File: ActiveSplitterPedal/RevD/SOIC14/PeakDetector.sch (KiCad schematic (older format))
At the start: 11 parts, among them U3 TL074

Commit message: Completed RevD
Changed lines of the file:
@@
 AR Path="/5F6A4453/5F3F63C2" Ref="U9"  Part="2"
 AR Path="/5F6AEF1B/5F3F63C2" Ref="U12"  Part="2"
-F 0 "U6" H 4025 2925 50  0000 C CNN
+F 0 "U12" H 4025 2925 50  0000 C CNN
 F 1 "TL074" H 4025 2825 50  0000 C CNN
 F 2 "Package_SO:SOIC-14_3.9x8.7mm_P1.27mm" H 4000 2625 50  0001 C CNN
@@
 AR Path="/5F6A4453/5F3F8AC2" Ref="U9"  Part="4"
 AR Path="/5F6AEF1B/5F3F8AC2" Ref="U12"  Part="4"
-F 0 "U6" H 7700 3092 50  0000 C CNN
+F 0 "U12" H 7700 3092 50  0000 C CNN
 F 1 "TL074" H 7700 3001 50  0000 C CNN
 F 2 "Package_SO:SOIC-14_3.9x8.7mm_P1.27mm" H 7650 2825 50  0001 C CNN
@@
 AR Path="/5F6A4453/5F3F9579" Ref="U9"  Part="5"
 AR Path="/5F6AEF1B/5F3F9579" Ref="U12"  Part="5"
-F 0 "U6" H 2650 6025 50  0000 R CNN
+F 0 "U12" H 2650 6025 50  0000 R CNN
 F 1 "TL074" H 2700 5925 50  0000 R CNN
 F 2 "Package_SO:SOIC-14_3.9x8.7mm_P1.27mm" H 2450 6075 50  0001 C CNN
@@
 AR Path="/5F6A4453/5F44F4A6" Ref="C27"  Part="1"
 AR Path="/5F6AEF1B/5F44F4A6" Ref="C38"  Part="1"
-F 0 "C16" H 3215 6671 50  0000 L CNN
+F 0 "C38" H 3215 6671 50  0000 L CNN
 F 1 "100nF" H 3215 6580 50  0000 L CNN
 F 2 "Capacitor_SMD:C_0805_2012Metric_Pad1.15x1.40mm_HandSolder" H 3138 6475 50  0001 C CNN
@@
 AR Path="/5F6A4453/5F45B6FE" Ref="C26"  Part="1"
 AR Path="/5F6AEF1B/5F45B6FE" Ref="C37"  Part="1"
-F 0 "C15" H 3215 5896 50  0000 L CNN
+F 0 "C37" H 3215 5896 50  0000 L CNN
 F 1 "100nF" H 3215 5805 50  0000 L CNN
 F 2 "Capacitor_SMD:C_0805_2012Metric_Pad1.15x1.40mm_HandSolder" H 3138 5700 50  0001 C CNN
@@
 AR Path="/5F6A4453/5F4B9375" Ref="D6"  Part="1"
 AR Path="/5F6AEF1B/5F4B9375" Ref="D8"  Part="1"
-F 0 "D4" V 8539 3207 50  0000 R CNN
+F 0 "D8" V 8539 3207 50  0000 R CNN
 F 1 "LED" V 8448 3207 50  0000 R CNN
 F 2 "LED_THT:LED_D5.0mm" H 8500 3325 50  0001 C CNN
@@
 AR Path="/5F6A4453/5F57D775" Ref="R14"  Part="1"
 AR Path="/5F6AEF1B/5F57D775" Ref="R20"  Part="1"
-F 0 "R8" V 4100 3075 50  0000 R CNN
+F 0 "R20" V 4100 3075 50  0000 R CNN
 F 1 "120K" V 3900 3125 50  0000 R CNN
 F 2 "Resistor_SMD:R_0805_2012Metric_Pad1.15x1.40mm_HandSolder" V 3930 3025 50  0001 C CNN
@@
 AR Path="/5F6A4453/5F58191C" Ref="R13"  Part="1"
 AR Path="/5F6AEF1B/5F58191C" Ref="R19"  Part="1"
-F 0 "R7" H 3800 3575 50  0000 R CNN
+F 0 "R19" H 3800 3575 50  0000 R CNN
 F 1 "1K" H 3800 3675 50  0000 R CNN
 F 2 "Resistor_SMD:R_0805_2012Metric_Pad1.15x1.40mm_HandSolder" V 3530 3625 50  0001 C CNN
@@
 AR Path="/5F6A4453/5F579AC3" Ref="R15"  Part="1"
 AR Path="/5F6AEF1B/5F579AC3" Ref="R21"  Part="1"
-F 0 "R9" H 8430 2879 50  0000 R CNN
+F 0 "R21" H 8430 2879 50  0000 R CNN
 F 1 "220R" H 8430 2970 50  0000 R CNN
 F 2 "Resistor_SMD:R_0805_2012Metric_Pad1.15x1.40mm_HandSolder" V 8430 2925 50  0001 C CNN
@@
 AR Path="/5F6A4453/5F5A1DE7" Ref="U9"  Part="3"
 AR Path="/5F6AEF1B/5F5A1DE7" Ref="U12"  Part="3"
-F 0 "U6" H 4850 5700 50  0000 C CNN
+F 0 "U12" H 4850 5700 50  0000 C CNN
 F 1 "TL074" H 4850 5800 50  0000 C CNN
 F 2 "Package_SO:SOIC-14_3.9x8.7mm_P1.27mm" H 4800 6200 50  0001 C CNN
@@
 AR Path="/5F6A4453/5F59995E" Ref="#PWR0128"  Part="1"
 AR Path="/5F6AEF1B/5F59995E" Ref="#PWR0140"  Part="1"
-F 0 "#PWR0116" H 3100 6675 50  0001 C CNN
+F 0 "#PWR0140" H 3100 6675 50  0001 C CNN
 F 1 "VCOM" H 3115 6998 50  0000 C CNN
 F 2 "" H 3100 6825 50  0001 C CNN
@@
 AR Path="/5F6A4453/5F599E65" Ref="#PWR0129"  Part="1"
 AR Path="/5F6AEF1B/5F599E65" Ref="#PWR0141"  Part="1"
-F 0 "#PWR0117" H 3600 3725 50  0001 C CNN
+F 0 "#PWR0141" H 3600 3725 50  0001 C CNN
 F 1 "VCOM" H 3615 4048 50  0000 C CNN
 F 2 "" H 3600 3875 50  0001 C CNN
@@
 AR Path="/5F6A4453/5F59A32D" Ref="#PWR0130"  Part="1"
 AR Path="/5F6AEF1B/5F59A32D" Ref="#PWR0142"  Part="1"
-F 0 "#PWR0118" H 6525 3725 50  0001 C CNN
+F 0 "#PWR0142" H 6525 3725 50  0001 C CNN
 F 1 "VCOM" H 6540 4048 50  0000 C CNN
 F 2 "" H 6525 3875 50  0001 C CNN
@@
 AR Path="/5F6A4453/5F59A89E" Ref="#PWR0131"  Part="1"
 AR Path="/5F6AEF1B/5F59A89E" Ref="#PWR0143"  Part="1"
-F 0 "#PWR0119" H 8500 3725 50  0001 C CNN
+F 0 "#PWR0143" H 8500 3725 50  0001 C CNN
 F 1 "VCOM" H 8515 4048 50  0000 C CNN
 F 2 "" H 8500 3875 50  0001 C CNN
@@
 AR Path="/5F6A4453/5F59CCEA" Ref="#PWR0132"  Part="1"
 AR Path="/5F6AEF1B/5F59CCEA" Ref="#PWR0144"  Part="1"
-F 0 "#PWR0120" H 2600 5100 50  0001 C CNN
+F 0 "#PWR0144" H 2600 5100 50  0001 C CNN
 F 1 "+3.3V" H 2615 5423 50  0000 C CNN
 F 2 "" H 2600 5250 50  0001 C CNN
@@
 AR Path="/5F6A4453/5F59E040" Ref="#PWR0133"  Part="1"
 AR Path="/5F6AEF1B/5F59E040" Ref="#PWR0145"  Part="1"
-F 0 "#PWR0121" H 2600 7000 50  0001 C CNN
+F 0 "#PWR0145" H 2600 7000 50  0001 C CNN
 F 1 "-3V3" H 2615 7073 50  0000 C CNN
 F 2 "" H 2600 6900 50  0001 C CNN
@@
 AR Path="/5F6A4453/5F59EC91" Ref="#PWR0134"  Part="1"
 AR Path="/5F6AEF1B/5F59EC91" Ref="#PWR0146"  Part="1"
-F 0 "#PWR0122" H 3100 5900 50  0001 C CNN
+F 0 "#PWR0146" H 3100 5900 50  0001 C CNN
 F 1 "VCOM" H 3115 6223 50  0000 C CNN
 F 2 "" H 3100 6050 50  0001 C CNN
@@
 AR Path="/5F6A4453/5F5E827F" Ref="D12"  Part="1"
 AR Path="/5F6AEF1B/5F5E827F" Ref="D13"  Part="1"
-F 0 "D11" H 5350 2958 50  0000 C CNN
+F 0 "D13" H 5350 2958 50  0000 C CNN
 F 1 "1N914" H 5350 3049 50  0000 C CNN
 F 2 "Diode_SMD:D_SOD-123F" H 5350 3175 50  0001 C CNN
@@
 AR Path="/5F6A4453/5F60D8BF" Ref="D5"  Part="1"
 AR Path="/5F6AEF1B/5F60D8BF" Ref="D7"  Part="1"
-F 0 "D3" H 6225 2408 50  0000 C CNN
+F 0 "D7" H 6225 2408 50  0000 C CNN
 F 1 "1N914" H 6225 2499 50  0000 C CNN
 F 2 "Diode_SMD:D_SOD-123F" H 6225 2625 50  0001 C CNN
@@
 AR Path="/5F6A4453/5F3F57C8" Ref="U9"  Part="1"
 AR Path="/5F6AEF1B/5F3F57C8" Ref="U12"  Part="1"
-F 0 "U6" H 5425 2850 50  0000 C CNN
+F 0 "U12" H 5425 2850 50  0000 C CNN
 F 1 "TL074" H 5425 2950 50  0000 C CNN
 F 2 "Package_SO:SOIC-14_3.9x8.7mm_P1.27mm" H 5325 2725 50  0001 C CNN
@@
 AR Path="/5F6A4453/5F5FC0EE" Ref="#PWR04"  Part="1"
 AR Path="/5F6AEF1B/5F5FC0EE" Ref="#PWR05"  Part="1"
-F 0 "#PWR03" H 6900 3725 50  0001 C CNN
+F 0 "#PWR05" H 6900 3725 50  0001 C CNN
 F 1 "VCOM" H 6915 4048 50  0000 C CNN
 F 2 "" H 6900 3875 50  0001 C CNN
@@
 AR Path="/5F6A4453/5F5FD306" Ref="R16"  Part="1"
 AR Path="/5F6AEF1B/5F5FD306" Ref="R22"  Part="1"
-F 0 "R10" H 6830 3354 50  0000 R CNN
+F 0 "R22" H 6830 3354 50  0000 R CNN
 F 1 "10M 1%" H 6830 3445 50  0000 R CNN
 F 2 "Resistor_SMD:R_0805_2012Metric_Pad1.15x1.40mm_HandSolder" V 6830 3400 50  0001 C CNN
@@
 AR Path="/5F6A4453/5F5AD5B8" Ref="C28"  Part="1"
 AR Path="/5F6AEF1B/5F5AD5B8" Ref="C39"  Part="1"
-F 0 "C17" H 6175 3450 50  0000 L CNN
+F 0 "C39" H 6175 3450 50  0000 L CNN
 F 1 "470uF 1%" H 6025 3350 50  0000 L CNN
 F 2 "Capacitor_SMD:C_1210_3225Metric_Pad1.42x2.65mm_HandSolder" H 6563 3250 50  0001 C CNN

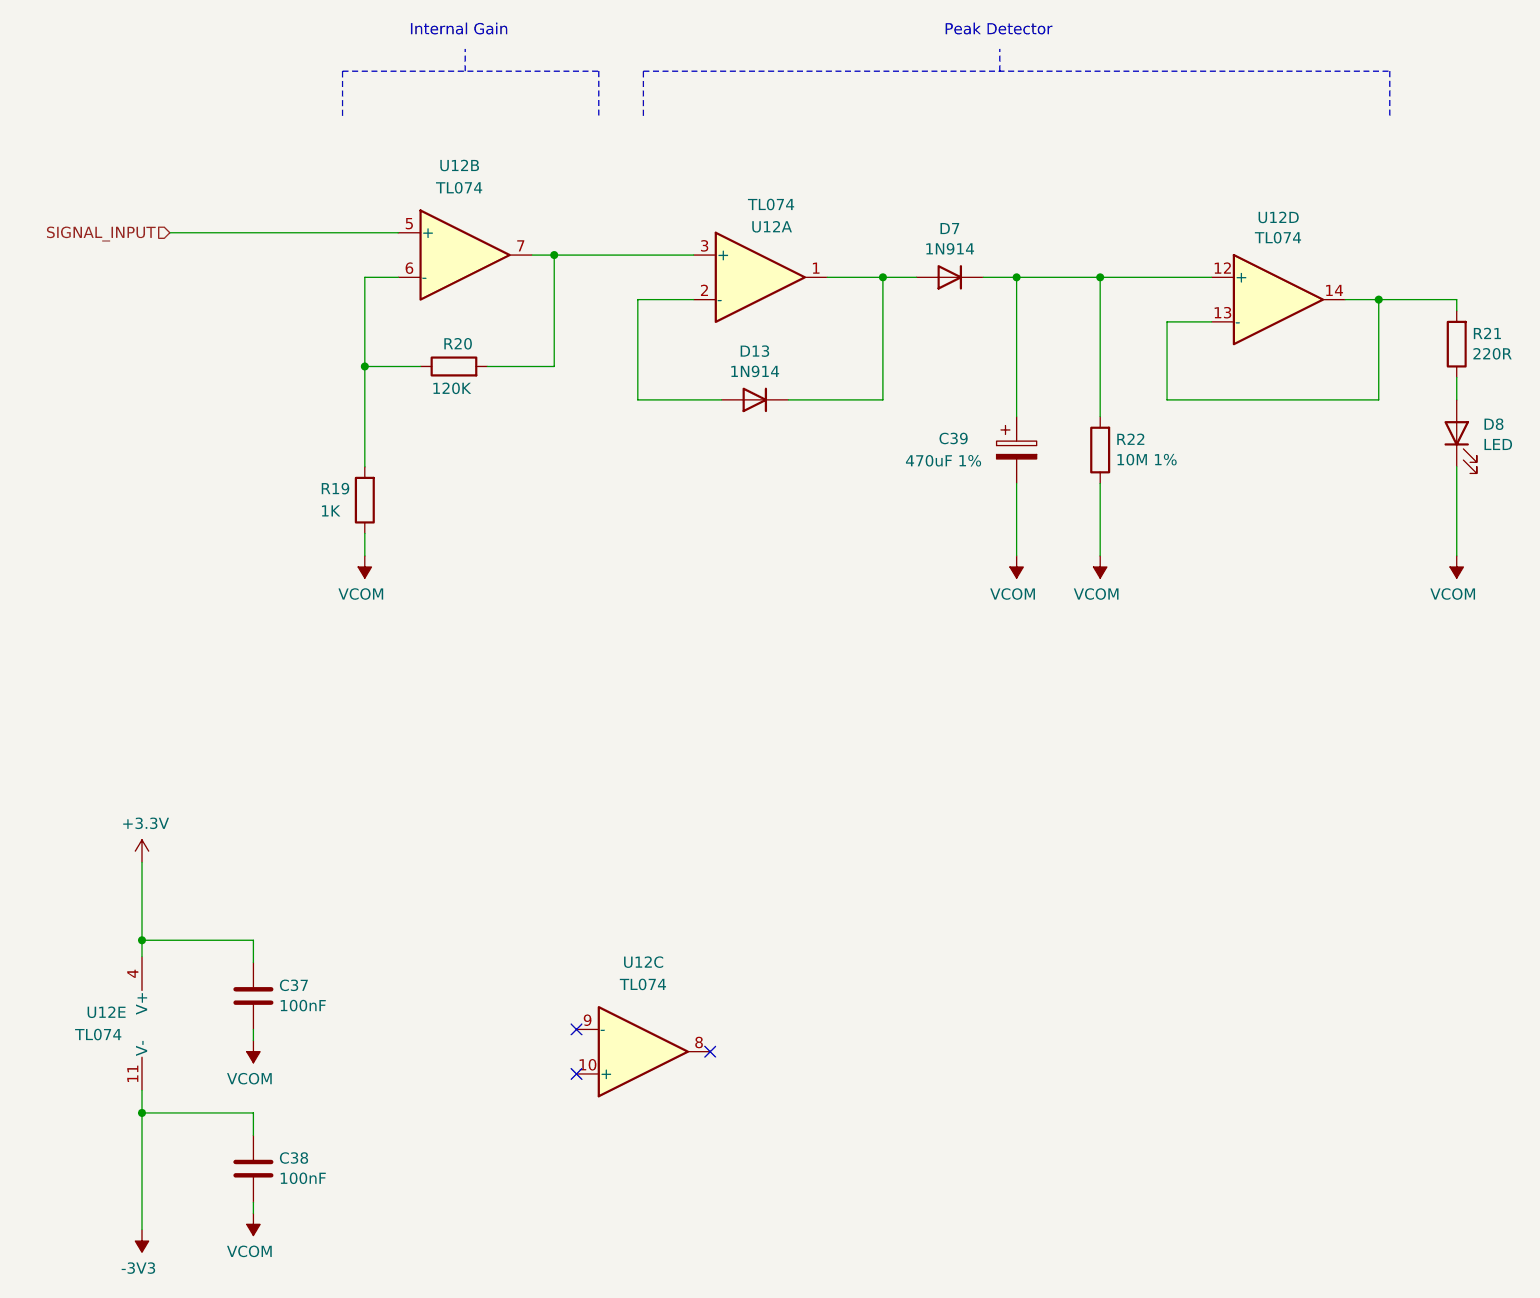
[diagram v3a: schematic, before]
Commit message: updated hw
- Changed peak detector gain feedback resistor to 10K
- Changed peak detector storage cap to 100nF
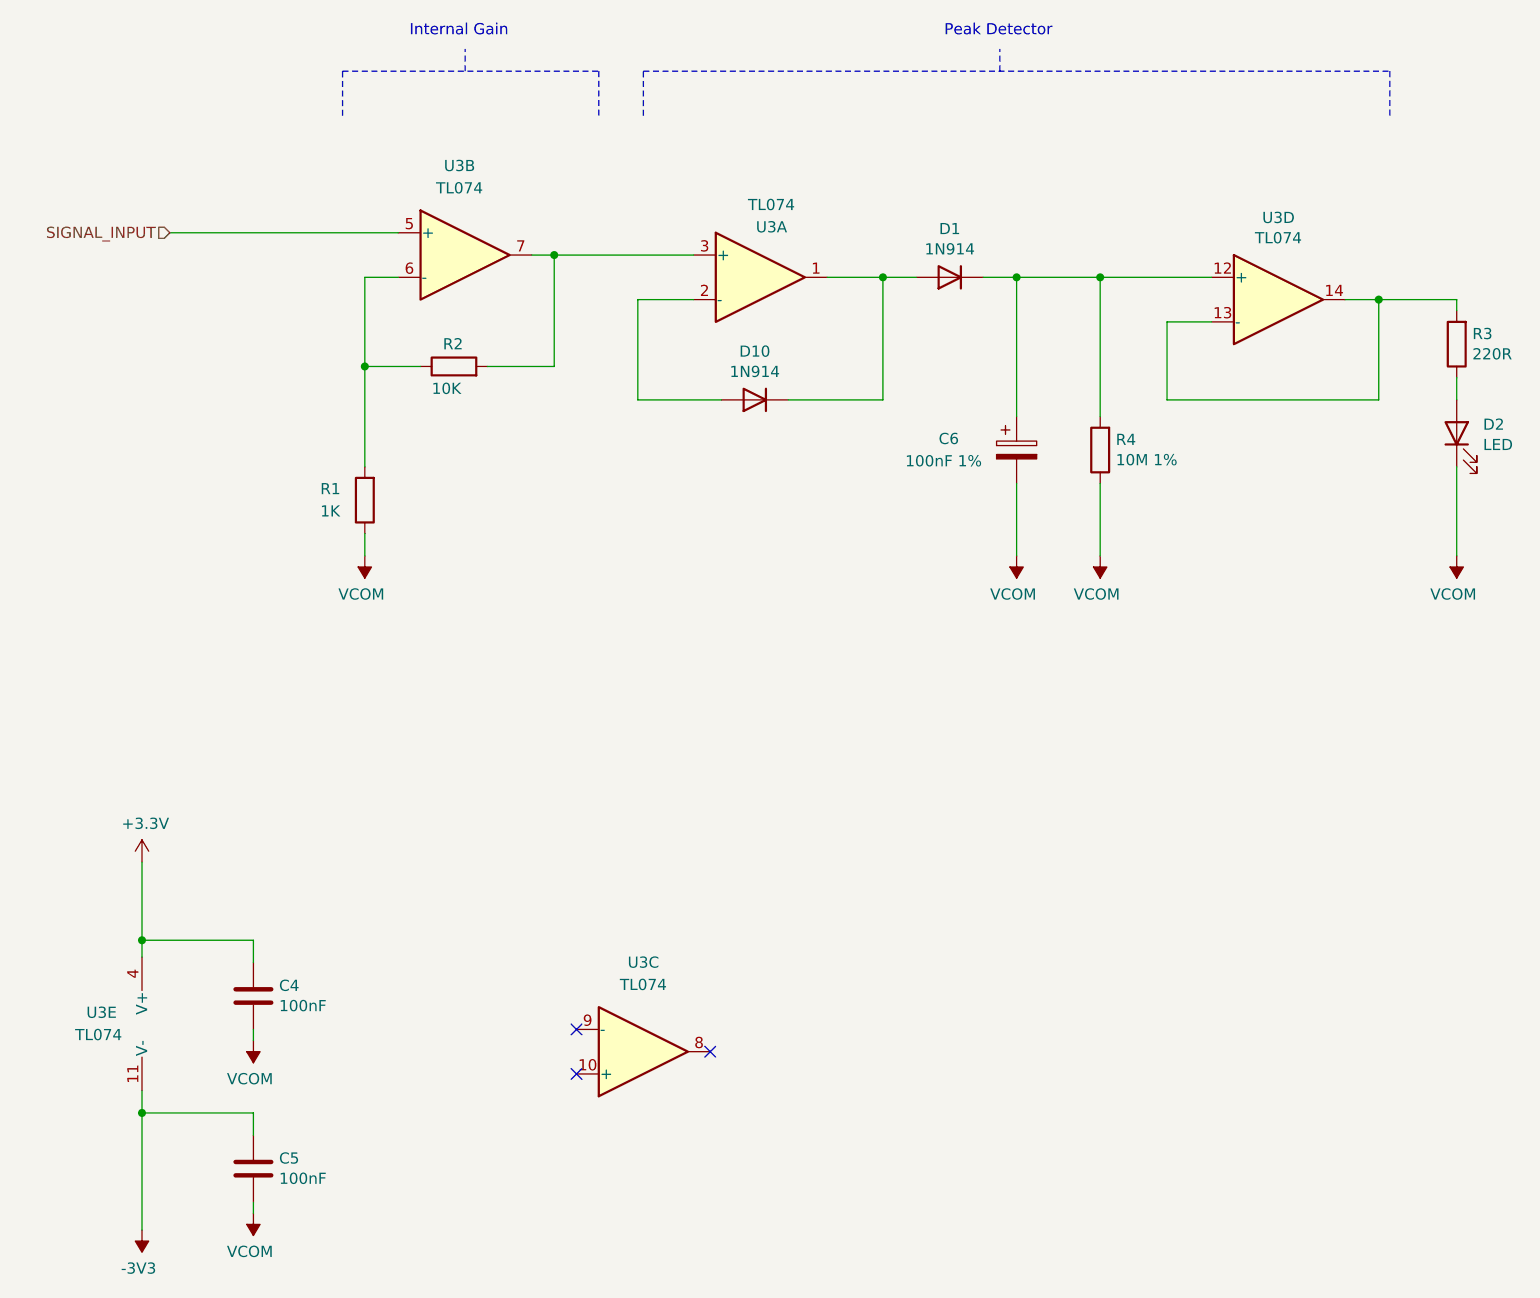
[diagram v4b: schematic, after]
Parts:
- C6: value 470uF 1% -> 100nF 1%
- R2: value 120K -> 10K
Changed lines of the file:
@@
 $Descr A4 11693 8268
 encoding utf-8
-Sheet 5 10
+Sheet 3 10
 Title ""
 Date ""
@@
 AR Path="/5F6A4453/5F3F63C2" Ref="U9"  Part="2"
 AR Path="/5F6AEF1B/5F3F63C2" Ref="U12"  Part="2"
-F 0 "U12" H 4025 2925 50  0000 C CNN
+F 0 "U3" H 4025 2925 50  0000 C CNN
 F 1 "TL074" H 4025 2825 50  0000 C CNN
 F 2 "Package_SO:SOIC-14_3.9x8.7mm_P1.27mm" H 4000 2625 50  0001 C CNN
@@
 AR Path="/5F6A4453/5F3F8AC2" Ref="U9"  Part="4"
 AR Path="/5F6AEF1B/5F3F8AC2" Ref="U12"  Part="4"
-F 0 "U12" H 7700 3092 50  0000 C CNN
+F 0 "U3" H 7700 3092 50  0000 C CNN
 F 1 "TL074" H 7700 3001 50  0000 C CNN
 F 2 "Package_SO:SOIC-14_3.9x8.7mm_P1.27mm" H 7650 2825 50  0001 C CNN
@@
 AR Path="/5F6A4453/5F3F9579" Ref="U9"  Part="5"
 AR Path="/5F6AEF1B/5F3F9579" Ref="U12"  Part="5"
-F 0 "U12" H 2650 6025 50  0000 R CNN
+F 0 "U3" H 2650 6025 50  0000 R CNN
 F 1 "TL074" H 2700 5925 50  0000 R CNN
 F 2 "Package_SO:SOIC-14_3.9x8.7mm_P1.27mm" H 2450 6075 50  0001 C CNN
@@
 AR Path="/5F6A4453/5F44F4A6" Ref="C27"  Part="1"
 AR Path="/5F6AEF1B/5F44F4A6" Ref="C38"  Part="1"
-F 0 "C38" H 3215 6671 50  0000 L CNN
+F 0 "C5" H 3215 6671 50  0000 L CNN
 F 1 "100nF" H 3215 6580 50  0000 L CNN
 F 2 "Capacitor_SMD:C_0805_2012Metric_Pad1.15x1.40mm_HandSolder" H 3138 6475 50  0001 C CNN
@@
 AR Path="/5F6A4453/5F45B6FE" Ref="C26"  Part="1"
 AR Path="/5F6AEF1B/5F45B6FE" Ref="C37"  Part="1"
-F 0 "C37" H 3215 5896 50  0000 L CNN
+F 0 "C4" H 3215 5896 50  0000 L CNN
 F 1 "100nF" H 3215 5805 50  0000 L CNN
 F 2 "Capacitor_SMD:C_0805_2012Metric_Pad1.15x1.40mm_HandSolder" H 3138 5700 50  0001 C CNN
@@
 AR Path="/5F6A4453/5F4B9375" Ref="D6"  Part="1"
 AR Path="/5F6AEF1B/5F4B9375" Ref="D8"  Part="1"
-F 0 "D8" V 8539 3207 50  0000 R CNN
+F 0 "D2" V 8539 3207 50  0000 R CNN
 F 1 "LED" V 8448 3207 50  0000 R CNN
 F 2 "LED_THT:LED_D5.0mm" H 8500 3325 50  0001 C CNN
@@
 AR Path="/5F6A4453/5F57D775" Ref="R14"  Part="1"
 AR Path="/5F6AEF1B/5F57D775" Ref="R20"  Part="1"
-F 0 "R20" V 4100 3075 50  0000 R CNN
-F 1 "120K" V 3900 3125 50  0000 R CNN
+F 0 "R2" V 4100 3075 50  0000 R CNN
+F 1 "10K" V 3900 3125 50  0000 R CNN
 F 2 "Resistor_SMD:R_0805_2012Metric_Pad1.15x1.40mm_HandSolder" V 3930 3025 50  0001 C CNN
 F 3 "~" H 4000 3025 50  0001 C CNN
@@
 AR Path="/5F6A4453/5F58191C" Ref="R13"  Part="1"
 AR Path="/5F6AEF1B/5F58191C" Ref="R19"  Part="1"
-F 0 "R19" H 3800 3575 50  0000 R CNN
+F 0 "R1" H 3800 3575 50  0000 R CNN
 F 1 "1K" H 3800 3675 50  0000 R CNN
 F 2 "Resistor_SMD:R_0805_2012Metric_Pad1.15x1.40mm_HandSolder" V 3530 3625 50  0001 C CNN
@@
 AR Path="/5F6A4453/5F579AC3" Ref="R15"  Part="1"
 AR Path="/5F6AEF1B/5F579AC3" Ref="R21"  Part="1"
-F 0 "R21" H 8430 2879 50  0000 R CNN
+F 0 "R3" H 8430 2879 50  0000 R CNN
 F 1 "220R" H 8430 2970 50  0000 R CNN
 F 2 "Resistor_SMD:R_0805_2012Metric_Pad1.15x1.40mm_HandSolder" V 8430 2925 50  0001 C CNN
@@
 AR Path="/5F6A4453/5F5A1DE7" Ref="U9"  Part="3"
 AR Path="/5F6AEF1B/5F5A1DE7" Ref="U12"  Part="3"
-F 0 "U12" H 4850 5700 50  0000 C CNN
+F 0 "U3" H 4850 5700 50  0000 C CNN
 F 1 "TL074" H 4850 5800 50  0000 C CNN
 F 2 "Package_SO:SOIC-14_3.9x8.7mm_P1.27mm" H 4800 6200 50  0001 C CNN
@@
 AR Path="/5F6A4453/5F59995E" Ref="#PWR0128"  Part="1"
 AR Path="/5F6AEF1B/5F59995E" Ref="#PWR0140"  Part="1"
-F 0 "#PWR0140" H 3100 6675 50  0001 C CNN
+F 0 "#PWR0104" H 3100 6675 50  0001 C CNN
 F 1 "VCOM" H 3115 6998 50  0000 C CNN
 F 2 "" H 3100 6825 50  0001 C CNN
@@
 AR Path="/5F6A4453/5F599E65" Ref="#PWR0129"  Part="1"
 AR Path="/5F6AEF1B/5F599E65" Ref="#PWR0141"  Part="1"
-F 0 "#PWR0141" H 3600 3725 50  0001 C CNN
+F 0 "#PWR0105" H 3600 3725 50  0001 C CNN
 F 1 "VCOM" H 3615 4048 50  0000 C CNN
 F 2 "" H 3600 3875 50  0001 C CNN
@@
 AR Path="/5F6A4453/5F59A32D" Ref="#PWR0130"  Part="1"
 AR Path="/5F6AEF1B/5F59A32D" Ref="#PWR0142"  Part="1"
-F 0 "#PWR0142" H 6525 3725 50  0001 C CNN
+F 0 "#PWR0106" H 6525 3725 50  0001 C CNN
 F 1 "VCOM" H 6540 4048 50  0000 C CNN
 F 2 "" H 6525 3875 50  0001 C CNN
@@
 AR Path="/5F6A4453/5F59A89E" Ref="#PWR0131"  Part="1"
 AR Path="/5F6AEF1B/5F59A89E" Ref="#PWR0143"  Part="1"
-F 0 "#PWR0143" H 8500 3725 50  0001 C CNN
+F 0 "#PWR0107" H 8500 3725 50  0001 C CNN
 F 1 "VCOM" H 8515 4048 50  0000 C CNN
 F 2 "" H 8500 3875 50  0001 C CNN
@@
 AR Path="/5F6A4453/5F59CCEA" Ref="#PWR0132"  Part="1"
 AR Path="/5F6AEF1B/5F59CCEA" Ref="#PWR0144"  Part="1"
-F 0 "#PWR0144" H 2600 5100 50  0001 C CNN
+F 0 "#PWR0108" H 2600 5100 50  0001 C CNN
 F 1 "+3.3V" H 2615 5423 50  0000 C CNN
 F 2 "" H 2600 5250 50  0001 C CNN
@@
 AR Path="/5F6A4453/5F59E040" Ref="#PWR0133"  Part="1"
 AR Path="/5F6AEF1B/5F59E040" Ref="#PWR0145"  Part="1"
-F 0 "#PWR0145" H 2600 7000 50  0001 C CNN
+F 0 "#PWR0109" H 2600 7000 50  0001 C CNN
 F 1 "-3V3" H 2615 7073 50  0000 C CNN
 F 2 "" H 2600 6900 50  0001 C CNN
@@
 AR Path="/5F6A4453/5F59EC91" Ref="#PWR0134"  Part="1"
 AR Path="/5F6AEF1B/5F59EC91" Ref="#PWR0146"  Part="1"
-F 0 "#PWR0146" H 3100 5900 50  0001 C CNN
+F 0 "#PWR0110" H 3100 5900 50  0001 C CNN
 F 1 "VCOM" H 3115 6223 50  0000 C CNN
 F 2 "" H 3100 6050 50  0001 C CNN
@@
 AR Path="/5F6A4453/5F5E827F" Ref="D12"  Part="1"
 AR Path="/5F6AEF1B/5F5E827F" Ref="D13"  Part="1"
-F 0 "D13" H 5350 2958 50  0000 C CNN
+F 0 "D10" H 5350 2958 50  0000 C CNN
 F 1 "1N914" H 5350 3049 50  0000 C CNN
 F 2 "Diode_SMD:D_SOD-123F" H 5350 3175 50  0001 C CNN
@@
 AR Path="/5F6A4453/5F60D8BF" Ref="D5"  Part="1"
 AR Path="/5F6AEF1B/5F60D8BF" Ref="D7"  Part="1"
-F 0 "D7" H 6225 2408 50  0000 C CNN
+F 0 "D1" H 6225 2408 50  0000 C CNN
 F 1 "1N914" H 6225 2499 50  0000 C CNN
 F 2 "Diode_SMD:D_SOD-123F" H 6225 2625 50  0001 C CNN
@@
 AR Path="/5F6A4453/5F3F57C8" Ref="U9"  Part="1"
 AR Path="/5F6AEF1B/5F3F57C8" Ref="U12"  Part="1"
-F 0 "U12" H 5425 2850 50  0000 C CNN
+F 0 "U3" H 5425 2850 50  0000 C CNN
 F 1 "TL074" H 5425 2950 50  0000 C CNN
 F 2 "Package_SO:SOIC-14_3.9x8.7mm_P1.27mm" H 5325 2725 50  0001 C CNN
@@
 AR Path="/5F6A4453/5F5FC0EE" Ref="#PWR04"  Part="1"
 AR Path="/5F6AEF1B/5F5FC0EE" Ref="#PWR05"  Part="1"
-F 0 "#PWR05" H 6900 3725 50  0001 C CNN
+F 0 "#PWR01" H 6900 3725 50  0001 C CNN
 F 1 "VCOM" H 6915 4048 50  0000 C CNN
 F 2 "" H 6900 3875 50  0001 C CNN
@@
 AR Path="/5F6A4453/5F5FD306" Ref="R16"  Part="1"
 AR Path="/5F6AEF1B/5F5FD306" Ref="R22"  Part="1"
-F 0 "R22" H 6830 3354 50  0000 R CNN
+F 0 "R4" H 6830 3354 50  0000 R CNN
 F 1 "10M 1%" H 6830 3445 50  0000 R CNN
 F 2 "Resistor_SMD:R_0805_2012Metric_Pad1.15x1.40mm_HandSolder" V 6830 3400 50  0001 C CNN
@@
 AR Path="/5F6A4453/5F5AD5B8" Ref="C28"  Part="1"
 AR Path="/5F6AEF1B/5F5AD5B8" Ref="C39"  Part="1"
-F 0 "C39" H 6175 3450 50  0000 L CNN
-F 1 "470uF 1%" H 6025 3350 50  0000 L CNN
+F 0 "C6" H 6175 3450 50  0000 L CNN
+F 1 "100nF 1%" H 6025 3350 50  0000 L CNN
 F 2 "Capacitor_SMD:C_1210_3225Metric_Pad1.42x2.65mm_HandSolder" H 6563 3250 50  0001 C CNN
 F 3 "~" H 6525 3400 50  0001 C CNN
